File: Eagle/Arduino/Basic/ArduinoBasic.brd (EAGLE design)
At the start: 100 x 80 mm, 6 parts

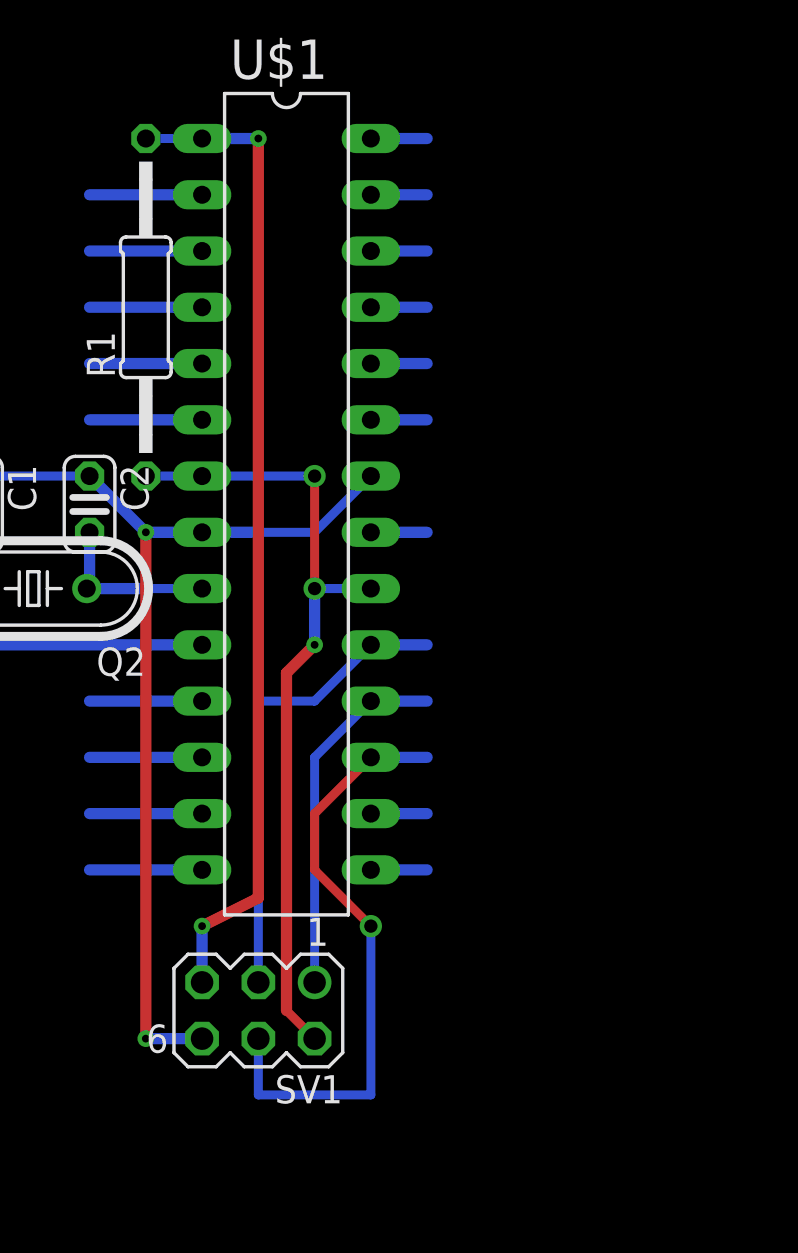
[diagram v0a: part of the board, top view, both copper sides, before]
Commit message: Arduino-Eagle boards easyer basic design
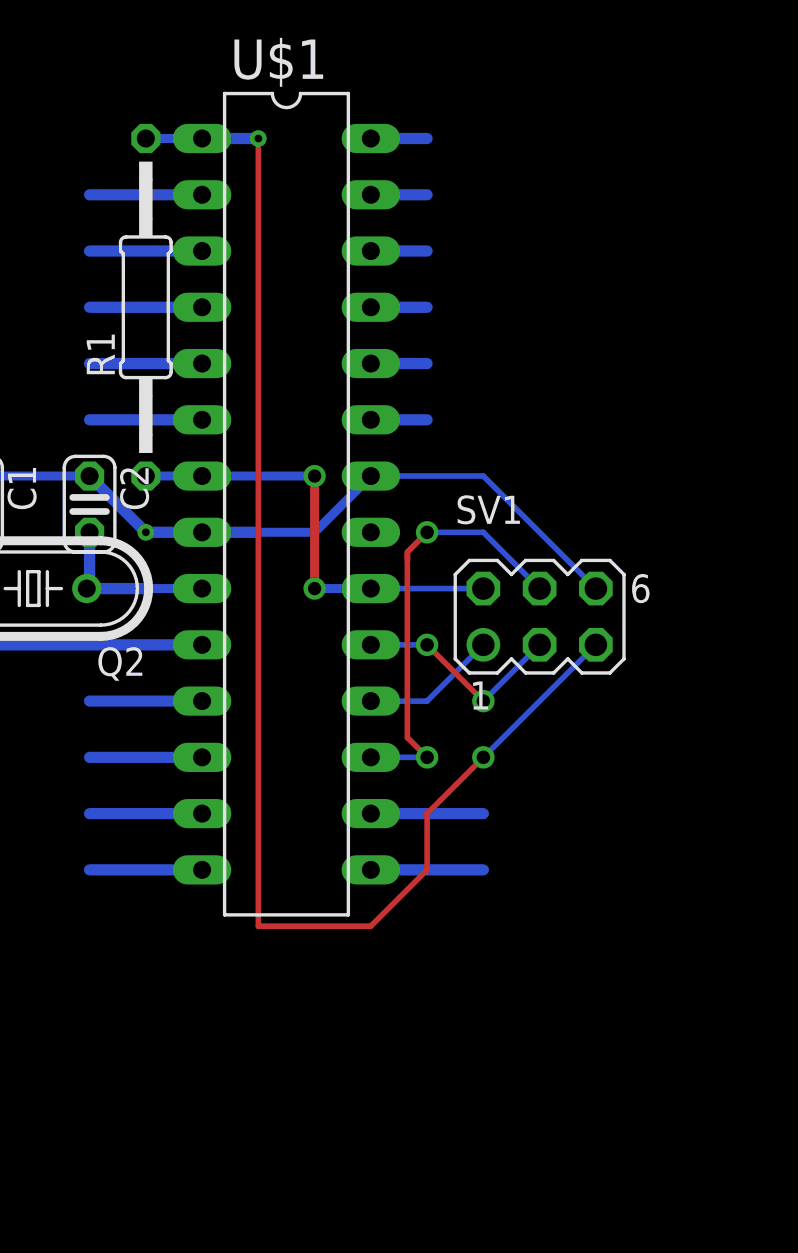
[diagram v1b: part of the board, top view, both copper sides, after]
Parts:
- moved SV1 21.8 mm to (58.4, 29.2), turned to 0 degrees
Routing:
- net RESET: track 44.7 -> 62.6 mm
- net VCC: track 36.6 -> 20.3 mm, vias 3 -> 2
- net DIO11(PWM)MOSI: track 27.5 -> 11.6 mm, vias 1 -> 2
- net GND: track 45.3 -> 32.1 mm, vias 2 -> 1
- net SCK[L5]: track 21.4 -> 9.72 mm, vias 0 -> 2
- net DIO12/MISO: track 16.3 -> 6.13 mm
- net N$1: track 0.00 -> 8.25 mm
- net AREF: track 2.54 -> 0.00 mm
- net DIO9(PWM): track 2.54 -> 5.08 mm
- net DIO10(PWM): track 2.54 -> 5.08 mm
